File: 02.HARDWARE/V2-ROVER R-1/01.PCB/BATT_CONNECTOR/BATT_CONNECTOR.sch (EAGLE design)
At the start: 15 parts, among them K1 FLEX11, Q1 DMG3415U-7

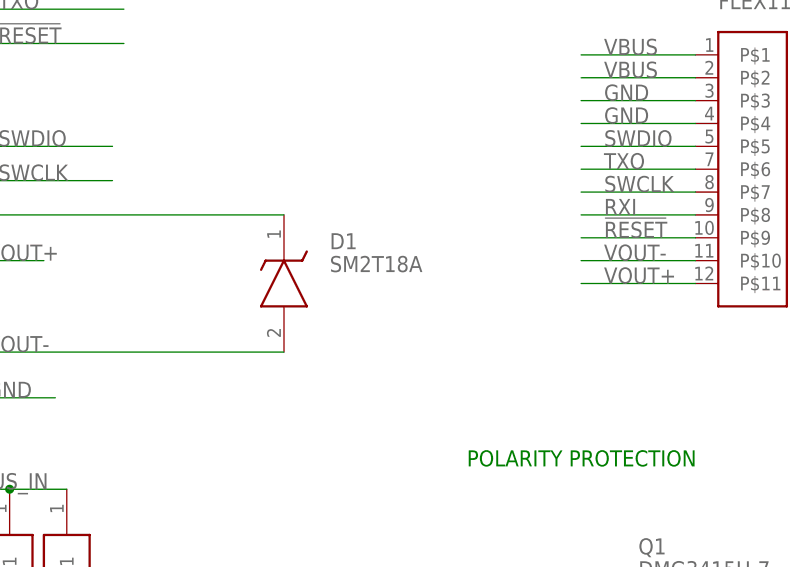
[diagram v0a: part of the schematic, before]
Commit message: Modificacion DCDC y Conector
DCDC: Posible version exclusiva PMU
Conector: Adatacion a cambio en produccion de un componente (SMJ)
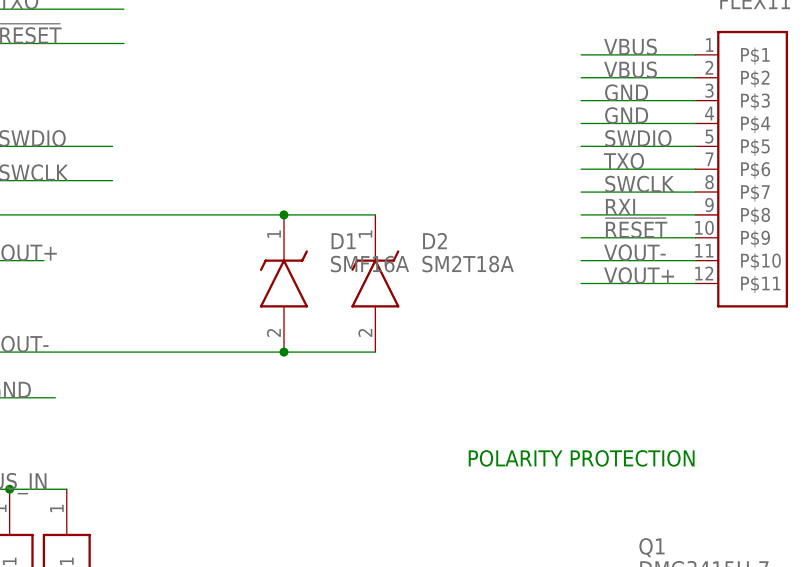
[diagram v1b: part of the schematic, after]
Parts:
- added D2: SM2T18A, SM2T18A:SM2T18A
- D1: value SM2T18A -> SMF16A; device SM2T18A:SM2T18A -> SMF16A:SMF16A
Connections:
- net VOUT+: now also D2.K
- net VOUT-: now also D2.A
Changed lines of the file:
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@@
 <part name="!RESET" library="testpad" library_urn="urn:adsk.eagle:library:385" deviceset="TP" device="B2,54" package3d_urn="urn:adsk.eagle:package:27948/1"/>
 <part name="TXO" library="testpad" library_urn="urn:adsk.eagle:library:385" deviceset="TP" device="B2,54" package3d_urn="urn:adsk.eagle:package:27948/1"/>
-<part name="D1" library="SM2T18A" deviceset="SM2T18A" device=""/>
+<part name="D1" library="SMF16A" deviceset="SMF16A" device=""/>
 <part name="RXI" library="testpad" library_urn="urn:adsk.eagle:library:385" deviceset="TP" device="B2,54" package3d_urn="urn:adsk.eagle:package:27948/1"/>
 <part name="Q1" library="SSM3J338R_LF" deviceset="SSM3J338R,LF" device="" value="DMG3415U-7"/>
+<part name="D2" library="SM2T18A" deviceset="SM2T18A" device=""/>
 </parts>
 <sheets>
@@
 <attribute name="VALUE" x="97.79" y="21.59" size="1.778" layer="96" align="center-left"/>
 </instance>
+<instance part="D2" gate="G$1" x="68.58" y="60.96" smashed="yes" rot="R270">
+<attribute name="NAME" x="73.66" y="57.15" size="1.778" layer="95"/>
+<attribute name="VALUE" x="73.66" y="54.61" size="1.778" layer="96"/>
+</instance>
 </instances>
 <busses>
@@
 <wire x1="58.42" y1="60.96" x2="21.59" y2="60.96" width="0.1524" layer="91"/>
 <junction x="21.59" y="60.96"/>
+<pinref part="D2" gate="G$1" pin="K"/>
+<wire x1="58.42" y1="60.96" x2="68.58" y2="60.96" width="0.1524" layer="91"/>
+<junction x="58.42" y="60.96"/>
 </segment>
 <segment>
@@
 <pinref part="D1" gate="G$1" pin="A"/>
 <wire x1="58.42" y1="45.72" x2="21.59" y2="45.72" width="0.1524" layer="91"/>
+<pinref part="D2" gate="G$1" pin="A"/>
+<wire x1="68.58" y1="45.72" x2="58.42" y2="45.72" width="0.1524" layer="91"/>
+<junction x="58.42" y="45.72"/>
 </segment>
 <segment>

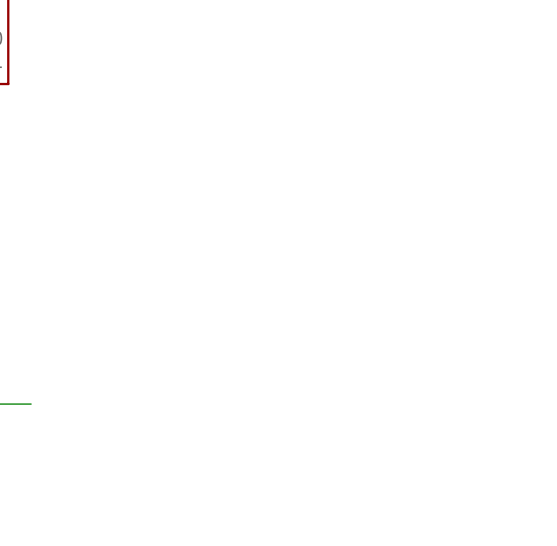
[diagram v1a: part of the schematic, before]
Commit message: Adiccion de Fiducidiales y actualizacion de Version
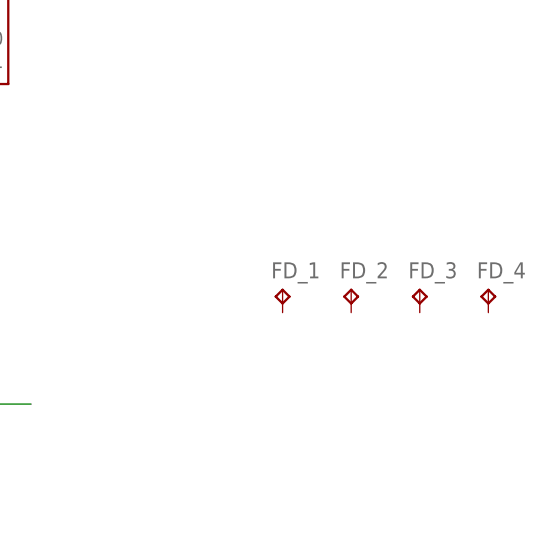
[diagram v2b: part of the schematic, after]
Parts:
- added FD_1, FD_2, FD_3, FD_4: FD_1, testpad:TPTP06SQ
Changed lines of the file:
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@@
 <part name="Q1" library="SSM3J338R_LF" deviceset="SSM3J338R,LF" device="" value="DMG3415U-7"/>
 <part name="D2" library="SM2T18A" deviceset="SM2T18A" device=""/>
+<part name="FD_1" library="testpad" library_urn="urn:adsk.eagle:library:385" deviceset="TP" device="TP06SQ" package3d_urn="urn:adsk.eagle:package:27952/1" value="FD_1"/>
+<part name="FD_2" library="testpad" library_urn="urn:adsk.eagle:library:385" deviceset="TP" device="TP06SQ" package3d_urn="urn:adsk.eagle:package:27952/1" value="FD_1"/>
+<part name="FD_3" library="testpad" library_urn="urn:adsk.eagle:library:385" deviceset="TP" device="TP06SQ" package3d_urn="urn:adsk.eagle:package:27952/1" value="FD_1"/>
+<part name="FD_4" library="testpad" library_urn="urn:adsk.eagle:library:385" deviceset="TP" device="TP06SQ" package3d_urn="urn:adsk.eagle:package:27952/1" value="FD_1"/>
 </parts>
 <sheets>
@@
 <attribute name="VALUE" x="73.66" y="54.61" size="1.778" layer="96"/>
 </instance>
+<instance part="FD_1" gate="G$1" x="144.78" y="27.94" smashed="yes">
+<attribute name="NAME" x="143.51" y="29.21" size="1.778" layer="95"/>
+<attribute name="TP_SIGNAL_NAME" x="146.05" y="26.67" size="1.778" layer="97"/>
+</instance>
+<instance part="FD_2" gate="G$1" x="152.4" y="27.94" smashed="yes">
+<attribute name="NAME" x="151.13" y="29.21" size="1.778" layer="95"/>
+<attribute name="TP_SIGNAL_NAME" x="153.67" y="26.67" size="1.778" layer="97"/>
+</instance>
+<instance part="FD_3" gate="G$1" x="160.02" y="27.94" smashed="yes">
+<attribute name="NAME" x="158.75" y="29.21" size="1.778" layer="95"/>
+<attribute name="TP_SIGNAL_NAME" x="161.29" y="26.67" size="1.778" layer="97"/>
+</instance>
+<instance part="FD_4" gate="G$1" x="167.64" y="27.94" smashed="yes">
+<attribute name="NAME" x="166.37" y="29.21" size="1.778" layer="95"/>
+<attribute name="TP_SIGNAL_NAME" x="168.91" y="26.67" size="1.778" layer="97"/>
+</instance>
 </instances>

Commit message: Nomenclatura de versiones
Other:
- note added: "BATTERY_CONNECTOR v2_Dic'23"
- note removed: "BATTERY_CONNECTOR"
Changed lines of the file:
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@@
 <plain>
 <text x="78.74" y="33.02" size="1.778" layer="91">POLARITY PROTECTION</text>
-<text x="58.42" y="106.68" size="2.54" layer="91">BATTERY_CONNECTOR</text>
+<text x="58.42" y="104.14" size="2.54" layer="91">BATTERY_CONNECTOR
+v2_Dic'23</text>
 </plain>
 <instances>
@@
 </drawing>
 <compatibility>
+<note version="6.3" minversion="6.2.2" severity="warning">
+Since Version 6.2.2 text objects can contain more than one line,
+which will not be processed correctly with this version.
+</note>
 <note version="8.2" severity="warning">
 Since Version 8.2, EAGLE supports online libraries. The ids

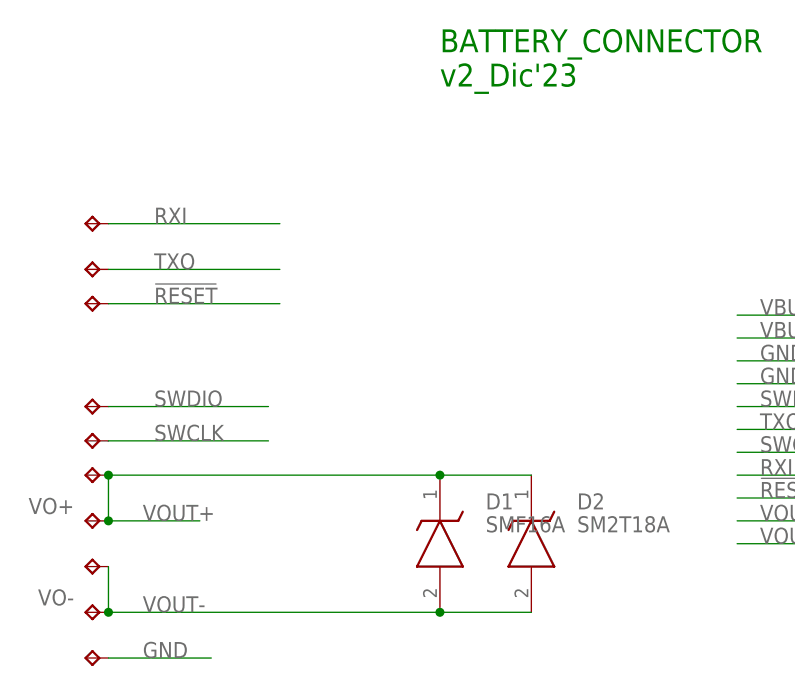
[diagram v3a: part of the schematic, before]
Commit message: MOSFET de Salida cerrado permanentemente #87.
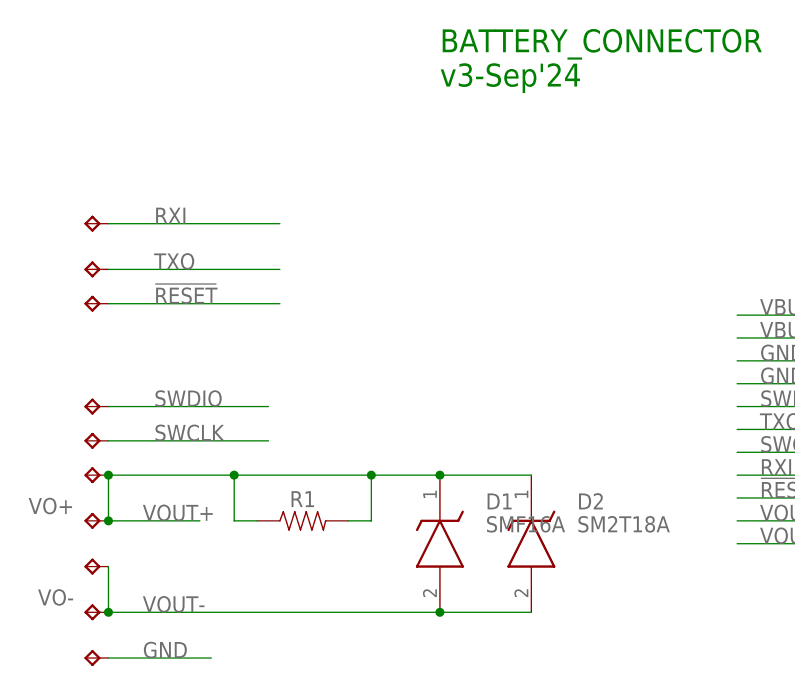
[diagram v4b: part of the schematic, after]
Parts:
- added R1: (no value), SparkFun-Resistors:RESISTOR0805
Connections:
- net VOUT+: now also R1.1, R1.2
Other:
- note added: "BATTERY_CONNECTOR v3-Sep'24"
- note removed: "BATTERY_CONNECTOR v2_Dic'23"
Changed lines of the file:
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@@
 <part name="FD_3" library="testpad" library_urn="urn:adsk.eagle:library:385" deviceset="TP" device="TP06SQ" package3d_urn="urn:adsk.eagle:package:27952/1" value="FD_1"/>
 <part name="FD_4" library="testpad" library_urn="urn:adsk.eagle:library:385" deviceset="TP" device="TP06SQ" package3d_urn="urn:adsk.eagle:package:27952/1" value="FD_1"/>
+<part name="R1" library="SparkFun-Resistors" library_urn="urn:adsk.eagle:library:532" deviceset="RESISTOR" device="0805" package3d_urn="urn:adsk.eagle:package:39651/1" value=" "/>
 </parts>
 <sheets>
@@
 <text x="78.74" y="33.02" size="1.778" layer="91">POLARITY PROTECTION</text>
 <text x="58.42" y="104.14" size="2.54" layer="91">BATTERY_CONNECTOR
-v2_Dic'23</text>
+v3-Sep'24</text>
 </plain>
 <instances>
@@
 <attribute name="TP_SIGNAL_NAME" x="168.91" y="26.67" size="1.778" layer="97"/>
 </instance>
+<instance part="R1" gate="G$1" x="43.18" y="55.88" smashed="yes">
+<attribute name="NAME" x="43.18" y="57.404" size="1.778" layer="95" font="vector" align="bottom-center"/>
+<attribute name="VALUE" x="43.18" y="54.356" size="1.778" layer="96" font="vector" align="top-center"/>
+</instance>
 </instances>
 <busses>
@@
 <label x="25.4" y="55.88" size="1.778" layer="95"/>
 <pinref part="D1" gate="G$1" pin="K"/>
-<wire x1="58.42" y1="60.96" x2="21.59" y2="60.96" width="0.1524" layer="91"/>
+<wire x1="58.42" y1="60.96" x2="50.8" y2="60.96" width="0.1524" layer="91"/>
 <junction x="21.59" y="60.96"/>
 <pinref part="D2" gate="G$1" pin="K"/>
+<wire x1="50.8" y1="60.96" x2="35.56" y2="60.96" width="0.1524" layer="91"/>
+<wire x1="35.56" y1="60.96" x2="21.59" y2="60.96" width="0.1524" layer="91"/>
 <wire x1="58.42" y1="60.96" x2="68.58" y2="60.96" width="0.1524" layer="91"/>
 <junction x="58.42" y="60.96"/>
+<pinref part="R1" gate="G$1" pin="2"/>
+<wire x1="48.26" y1="55.88" x2="50.8" y2="55.88" width="0.1524" layer="91"/>
+<wire x1="50.8" y1="55.88" x2="50.8" y2="60.96" width="0.1524" layer="91"/>
+<junction x="50.8" y="60.96"/>
+<pinref part="R1" gate="G$1" pin="1"/>
+<wire x1="38.1" y1="55.88" x2="35.56" y2="55.88" width="0.1524" layer="91"/>
+<wire x1="35.56" y1="55.88" x2="35.56" y2="60.96" width="0.1524" layer="91"/>
+<junction x="35.56" y="60.96"/>
 </segment>
 <segment>

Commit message: Connectores. Se añaden PADs para señales de comunicacion.
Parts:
- removed R1: (no value), SparkFun-Resistors:RESISTOR0805
- removed VOUT+1, VOUT-1: TPB2,54, testpad:TPB2,54
- added DAT, ID: TPB2,54, testpad:TPB2,54
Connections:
- net SWCLK: now also ID.TP
- net SWDIO: now also DAT.TP
- net VOUT+: no longer R1.1, R1.2, VOUT+1.TP
- net VOUT-: no longer VOUT-1.TP
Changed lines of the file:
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@@
 <part name="GND" library="testpad" library_urn="urn:adsk.eagle:library:385" deviceset="TP" device="B2,54" package3d_urn="urn:adsk.eagle:package:27948/1"/>
 <part name="K1" library="Flex_3mm" deviceset="FLEX11" device=""/>
-<part name="VOUT+1" library="testpad" library_urn="urn:adsk.eagle:library:385" deviceset="TP" device="B2,54" package3d_urn="urn:adsk.eagle:package:27948/1"/>
-<part name="VOUT-1" library="testpad" library_urn="urn:adsk.eagle:library:385" deviceset="TP" device="B2,54" package3d_urn="urn:adsk.eagle:package:27948/1"/>
 <part name="H1" library="S1761-42R" deviceset="S1761-42R" device=""/>
 <part name="H2" library="S1761-42R" deviceset="S1761-42R" device=""/>
@@
 <part name="FD_3" library="testpad" library_urn="urn:adsk.eagle:library:385" deviceset="TP" device="TP06SQ" package3d_urn="urn:adsk.eagle:package:27952/1" value="FD_1"/>
 <part name="FD_4" library="testpad" library_urn="urn:adsk.eagle:library:385" deviceset="TP" device="TP06SQ" package3d_urn="urn:adsk.eagle:package:27952/1" value="FD_1"/>
-<part name="R1" library="SparkFun-Resistors" library_urn="urn:adsk.eagle:library:532" deviceset="RESISTOR" device="0805" package3d_urn="urn:adsk.eagle:package:39651/1" value=" "/>
+<part name="ID" library="testpad" library_urn="urn:adsk.eagle:library:385" deviceset="TP" device="B2,54" package3d_urn="urn:adsk.eagle:package:27948/1"/>
+<part name="DAT" library="testpad" library_urn="urn:adsk.eagle:library:385" deviceset="TP" device="B2,54" package3d_urn="urn:adsk.eagle:package:27948/1"/>
 </parts>
 <sheets>
@@
 <attribute name="NAME" x="106.68" y="86.82" size="1.778" layer="95"/>
 <attribute name="VALUE" x="106.68" y="83.82" size="1.778" layer="96"/>
-</instance>
-<instance part="VOUT+1" gate="G$1" x="19.05" y="60.96" smashed="yes" rot="R90">
-<attribute name="TP_SIGNAL_NAME" x="20.32" y="62.23" size="1.778" layer="97" rot="R90"/>
-</instance>
-<instance part="VOUT-1" gate="G$1" x="19.05" y="50.8" smashed="yes" rot="R90">
-<attribute name="TP_SIGNAL_NAME" x="20.32" y="52.07" size="1.778" layer="97" rot="R90"/>
 </instance>
 <instance part="H1" gate="G$1" x="34.29" y="30.48" smashed="yes" rot="R270"/>
@@
 <attribute name="TP_SIGNAL_NAME" x="168.91" y="26.67" size="1.778" layer="97"/>
 </instance>
-<instance part="R1" gate="G$1" x="43.18" y="55.88" smashed="yes">
-<attribute name="NAME" x="43.18" y="57.404" size="1.778" layer="95" font="vector" align="bottom-center"/>
-<attribute name="VALUE" x="43.18" y="54.356" size="1.778" layer="96" font="vector" align="top-center"/>
+<instance part="ID" gate="G$1" x="19.05" y="96.52" smashed="yes" rot="R90">
+<attribute name="TP_SIGNAL_NAME" x="20.32" y="97.79" size="1.778" layer="97" rot="R90"/>
+</instance>
+<instance part="DAT" gate="G$1" x="19.05" y="104.14" smashed="yes" rot="R90">
+<attribute name="TP_SIGNAL_NAME" x="20.32" y="105.41" size="1.778" layer="97" rot="R90"/>
 </instance>
 </instances>
@@
 <net name="VOUT+" class="0">
 <segment>
-<pinref part="VOUT+1" gate="G$1" pin="TP"/>
 <pinref part="VO+" gate="G$1" pin="TP"/>
 <wire x1="21.59" y1="60.96" x2="21.59" y2="55.88" width="0.1524" layer="91"/>
@@
 <label x="25.4" y="55.88" size="1.778" layer="95"/>
 <pinref part="D1" gate="G$1" pin="K"/>
-<wire x1="58.42" y1="60.96" x2="50.8" y2="60.96" width="0.1524" layer="91"/>
-<junction x="21.59" y="60.96"/>
+<wire x1="58.42" y1="60.96" x2="21.59" y2="60.96" width="0.1524" layer="91"/>
 <pinref part="D2" gate="G$1" pin="K"/>
-<wire x1="50.8" y1="60.96" x2="35.56" y2="60.96" width="0.1524" layer="91"/>
-<wire x1="35.56" y1="60.96" x2="21.59" y2="60.96" width="0.1524" layer="91"/>
 <wire x1="58.42" y1="60.96" x2="68.58" y2="60.96" width="0.1524" layer="91"/>
 <junction x="58.42" y="60.96"/>
-<pinref part="R1" gate="G$1" pin="2"/>
-<wire x1="48.26" y1="55.88" x2="50.8" y2="55.88" width="0.1524" layer="91"/>
-<wire x1="50.8" y1="55.88" x2="50.8" y2="60.96" width="0.1524" layer="91"/>
-<junction x="50.8" y="60.96"/>
-<pinref part="R1" gate="G$1" pin="1"/>
-<wire x1="38.1" y1="55.88" x2="35.56" y2="55.88" width="0.1524" layer="91"/>
-<wire x1="35.56" y1="55.88" x2="35.56" y2="60.96" width="0.1524" layer="91"/>
-<junction x="35.56" y="60.96"/>
 </segment>
 <segment>
@@
 <net name="VOUT-" class="0">
 <segment>
-<pinref part="VOUT-1" gate="G$1" pin="TP"/>
 <pinref part="VO-" gate="G$1" pin="TP"/>
 <wire x1="21.59" y1="50.8" x2="21.59" y2="45.72" width="0.1524" layer="91"/>
@@
 <pinref part="K1" gate="G$1" pin="P$7"/>
 </segment>
+<segment>
+<pinref part="ID" gate="G$1" pin="TP"/>
+<wire x1="21.59" y1="96.52" x2="35.56" y2="96.52" width="0.1524" layer="91"/>
+<label x="25.4" y="96.52" size="1.778" layer="95"/>
+</segment>
 </net>
 <net name="SWDIO" class="0">
@@
 <pinref part="K1" gate="G$1" pin="P$5"/>
 </segment>
+<segment>
+<pinref part="DAT" gate="G$1" pin="TP"/>
+<wire x1="21.59" y1="104.14" x2="38.1" y2="104.14" width="0.1524" layer="91"/>
+<label x="25.4" y="104.14" size="1.778" layer="95"/>
+</segment>
 </net>
